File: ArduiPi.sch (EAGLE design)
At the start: 59 parts, among them IC1 DS2482-100S, IC2 AVR-MEGA8-PPTH, J1 VIN, J3 ISP, Q1 BS170, Q2 BS170, Q3 BS170, Q4 BS170, U1 LD1117 3V3, U2 78M05, U3 TXB0108, U4 TXB0108, Y1 16MHz

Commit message: Final Design
Final Design
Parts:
- removed $0000002: 22pF, SparkFun:CAPPTH2
- removed $5: 0.1uF, SparkFun:CAPPTH2
- removed JP3: PI I/O, adafruit:PINHD-1X8BIG
- removed JP4: 1-Wire, adafruit:PINHD-1X3
- removed P1, P2: (no value), Seeedstudio-Discreter.rpt:PAD-SOLDERJUMPER-2WAYT
- removed R13, R20: 10k, SparkFun:RESISTORAXIAL-0.3
- removed RASPBERRY: RASPBERRYPI_BB, microbuilder:RASPBERRYPI_BB
- removed S1: RESET, SparkFun:TAC_SWITCHPTH
- removed SERIAL-ARDUINO, SERIAL-PI: GROVE, Connector:TWIG-2.0-LEADED
- removed Y1: 16MHz, SparkFun:CRYSTALHC49US
- added ARDUINO-SERIAL, PI-SERIAL: GROVE, Connector:TWIG-2.0-LEADED
- added C13, C14, C15, C16: 0.1uF, resistor:C-EUC0603
- added D1: 1N4004, adafruit:1N4004
- added I2C-OLED, PC1, POWER: DNP, Seeedstudio-Connector:HEADER-6P-2.54
- added J10: ICSP, SparkFun:AVR_SPI_PRG_6PTH
- added J11: DNP, Seeedstudio-Connector:HEADER-4P-80/40MIL
- added J12, J13, PB1, PD1, SPI-OLED, SPI-OLED-PI: DNP, Seeedstudio-Connector:HEADER-8P-2.54
- added J2, J4, J5, J6, J7, J8: DNP, Seeedstudio-Connector:HEADER-3P-2.54
- added J9: DC-044-AH, For_Test_Albert:DC-044
- added K1: RESET, Seeedstudio-Discrete.rpt:BOTTON-2P-90
- added LED1: BLUE, led:LEDCHIP-LED0603
- added LED2: RED, led:LEDCHIP-LED0603
- added PAD1: PAD1, Seeedstudio-Discreter.rpt:PAD-SOLDERJUMPER-2WAYS
- added PAD2: PAD0, Seeedstudio-Discreter.rpt:PAD-SOLDERJUMPER-2WAYS
- added PI-P1: PI-P1, pi:RASPBERRYPI_BV2
- added PLED1: PLED1, Seeedstudio-Discreter.rpt:PAD-SOLDERJUMPER-2WAYS
- added PLED2: PLED2, Seeedstudio-Discreter.rpt:PAD-SOLDERJUMPER-2WAYS
- added PSSPI: PSSPI, Seeedstudio-Discreter.rpt:PAD-SOLDERJUMPER-2WAYS
- added PVDD: PVDD, Seeedstudio-Discreter.rpt:PAD-SOLDERJUMPERNC
- added Q5: BSS84, transistor-small-signal:BSS84
- added R10: 180, resistor:R-EU_R0805
- added R4: 4.7K, resistor:R-EU_R0805
- added R7, R8: 10k, resistor:R-EU_R0603
- added R9: 120, resistor:R-EU_R0805
- added U5: TXB0108, adafruit:TXB0108PWR
- C1: value 47uF -> 0.1uF; device SparkFun:CAP_POLPTH1 -> Seeedstudio-Discrete.rpt:C'1.4'
- C10: value 22pF -> 0.1uF; device SparkFun:CAPPTH2 -> Seeedstudio-Discrete.rpt:C'1.4'
- C11, C12: device SparkFun:CAPPTH2 -> resistor:C-EUC0603
- C2, C3: value 0.1uF -> 22pF; device SparkFun:CAPPTH2 -> Seeedstudio-Discrete.rpt:C'1.4'
- C4, C5, C8: device SparkFun:CAPPTH2 -> Seeedstudio-Discrete.rpt:C'1.4'
- C6: value 0.1uF -> 47uF; device SparkFun:CAPPTH2 -> SparkFun:CAP_POLPTH2
- C7: value 0.1uF -> 10uF; device SparkFun:CAPPTH2 -> SparkFun:CAP_POLPTH2
- C9: value 10uF -> 0.1uF; device SparkFun:CAP_POLPTH1 -> resistor:C-EUC0603
- IC1: value DS2482-100S -> AVR-MEGA8-PPTH; device 1wire:DS2482-100S -> SparkFun:AVR-MEGA8-PPTH
- IC2: value AVR-MEGA8-PPTH -> DS2482-100S; device SparkFun:AVR-MEGA8-PPTH -> 1wire:DS2482-100S
- J1: value VIN -> Teleinfo; device SparkFun:POWER_JACKPTH_LOCK -> Seeedstudio-Connector:HEADER-2P-2.54
- J3: value ISP -> DNP; device SparkFun:AVR_SPI_PRG_6PTH -> Seeedstudio-Connector:HEADER-3P-2.54
- JP2: value PI I/O -> 1-Wire; device adafruit:PINHD-1X8BIG -> adafruit:PINHD-1X3
- PCLK: value (none) -> PCLK
- PMISO: value (none) -> PMISO
- PMOSI: value (none) -> PMOSI
- PRX: value (none) -> PRX
- PSCL: value (none) -> PSCL
- PSDA: value (none) -> PSDA
- PSS: value (none) -> PSS; device Seeedstudio-Discreter.rpt:PAD-SOLDERJUMPERNC -> Seeedstudio-Discreter.rpt:PAD-SOLDERJUMPER-2WAYS
- PTX: value (none) -> PTX
- Q1, Q2, Q3, Q4: value BS170 -> BSS138; device transistor-small-signal:BS170 -> Seeedstudio-Discreter.rpt:MOSFET-N-SOT23
- R1: value 10k -> 1.2k; device SparkFun:RESISTORAXIAL-0.3 -> resistor:R-EU_R0805
- R2: value 1.2k -> 10k; device SparkFun:RESISTORAXIAL-0.3 -> resistor:R-EU_R0805
- R3: device SparkFun:RESISTORAXIAL-0.3 -> resistor:R-EU_R0805
- R5: value 10k -> 4.7K; device SparkFun:RESISTORAXIAL-0.3 -> resistor:R-EU_R0805
- R6: device SparkFun:RESISTORAXIAL-0.3 -> resistor:R-EU_R0603
- STINFO: value (none) -> STINFO; device Seeedstudio-Discreter.rpt:PAD-SOLDERJUMPER-2WAYT -> Seeedstudio-Discreter.rpt:PAD-SOLDERJUMPER-2WAYS
- U1: value LD1117 3V3 -> 78M05; device Seeedstudio-IC:LD1117SOT223 -> SeedStudio-IC:78M05-TO252
- U2: value 78M05 -> LD1117 3V3; device SeedStudio-IC:78M05-TO252 -> Seeedstudio-IC:LD1117SOT223
- U3: value TXB0108 -> TXB0104; device adafruit:TXB0108PWR -> adafruit:TXB0104PWR
- X1: value (none) -> 16Mhz; device _c2h:CON-CLAMP-2 -> Seeedstudio-Discrete.rpt:CRYSTAL-HC49S
- renumbered SCL to PSCL, SDA to PSDA
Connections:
- new net GPIO28: PI-P1.GPIO8, U3.A1
- new net GPIO29: PI-P1.GPIO9, U3.A2
- new net GPIO30: PI-P1.GPIO10, U3.A3
- new net GPIO31: PI-P1.GPIO11, U3.A4
- new net IO28: J11.P$1, U3.B1
- new net IO29: J11.P$2, U3.B2
- new net IO30: J11.P$3, U3.B3
- new net IO31: J11.P$4, U3.B4
- new net N$14: J1.2, R1.2
- new net N$15: IC2G$1.PCT, Q5.G
- new net N$16: PLED1.2, R9.1
- new net N$17: LED1.A, R9.2
- new net N$18: LED2.A, R10.2
- new net N$19: R6.1, U3.OE
- new net N$20: PLED2.2, R10.1
- new net SSPI: PSSPI.2, SPI-OLED-PI.8
- net 3V3: now also POWER.5
- net 3V3-EXT: now also C10.2, U2.OUT, U2.TAB; no longer C7.1, U1.TAB
- net 3V3-PI: now also C11.1, C12.1, C13.1, PI-P1.3.3V@1, PI-P1.3.3V@2, Q3.G, R7.2, R8.2, U5.VCCA; no longer C2.1, C3.1, Q2.G, R5.2, RASPBERRY.3V3-PI
- net 5V-EXT: now also C7.+, C8.2, PLED2.1, PVDD.2, U1.OUT, U2.IN; no longer C12.1, C9.+, U1.IN, U2.OUT
- net 5V-PI: now also PI-P1.5.0V@1, PI-P1.5.0V@2, PLED2.3; no longer RASPBERRY.5V-PI
- net AD0: now also IC1.PC0(ADC0), PC1.1; no longer IC2.PC0(ADC0)
- net AD1: now also IC1.PC1(ADC1), PC1.2; no longer IC2.PC1(ADC1)
- net AD2: now also IC1.PC2(ADC2), PC1.3; no longer IC2.PC2(ADC2)
- net AD3: now also IC1.PC3(ADC3), PC1.4; no longer IC2.PC3(ADC3)
- net AD4/SDA: now also IC1.PC4(ADC4/SDA), PC1.5; no longer IC2.PC4(ADC4/SDA)
- net AD5/SCL: now also IC1.PC5(ADC5/SCL), PC1.6; no longer IC2.PC5(ADC5/SCL)
- net AREF: now also C5.2, PB1.8; no longer C11.1
- net CE0: now also J13.6, PSS.3, PSSPI.3, U5.B6; no longer JP3.6, PSS.1, U4.B6
- net CE1: now also J13.7, PSS.1, PSSPI.1, U5.B7; no longer JP3.7, U4.B7
- net CE3: now also J13.8, U5.B8; no longer JP3.8, U4.B8
- net D0/RX-I: now also ARDUINO-SERIAL.1, IC1.PD0(RXD), PD1.1; no longer IC2.PD0(RXD)
- net D1/TX-O: now also ARDUINO-SERIAL.2, IC1.PD1(TXD), PD1.2; no longer IC2.PD1(TXD)
- net D10/SS: now also IC1.PB2(SS/OC1B), J6.P$3, PB1.3, SPI-OLED.8; no longer IC2.PB2(SS/OC1B)
- net D11/MOSI: now also IC1.PB3(MOSI/OC2), J10.4, J7.P$3, PB1.4, SPI-OLED.4; no longer IC2.PB3(MOSI/OC2), J3.4
- net D12/MISO: now also IC1.PB4(MISO), J10.1, PB1.5; no longer IC2.PB4(MISO), J3.1
- net D13/SCK: now also IC1.PB5(SCK), J10.3, PB1.6, PLED1.1, SPI-OLED.5; no longer IC2.PB5(SCK), J3.3
- net D2: now also IC1.PD2(INT0), PD1.3, PLED1.3; no longer IC2.PD2(INT0)
- net D3: now also IC1.PD3(INT1), J2.P$3, PD1.4; no longer IC2.PD3(INT1)
- net D4: now also I2C-OLED.4, IC1.PD4(XCK/T0), PD1.5; no longer IC2.PD4(XCK/T0)
- net D5: now also IC1.PD5(T1), J3.P$3, PD1.6; no longer IC2.PD5(T1)
- net D6: now also IC1.PD6(AIN0), J4.P$3, PD1.7; no longer IC2.PD6(AIN0)
- net D7: now also IC1.PD7(AIN1), PD1.8, SPI-OLED.7; no longer IC2.PD7(AIN1)
- net D8: now also IC1.PB0(ICP), PB1.1, SPI-OLED.6; no longer IC2.PB0(ICP)
- net D9: now also IC1.PB1(OC1A), J5.P$3, PB1.2; no longer IC2.PB1(OC1A)
- net DTR: now also C1.2; no longer C8.1
- net GND: now also ARDUINO-SERIAL.4, C13.2, C14.2, C15.2, C16.2, C6.-, C7.-, C8.1, C9.2, I2C-OLED.3, IC1.AGND, IC1.GND@1, IC2P.GND, J10.6, J2.P$2, J3.P$2, J4.P$2, J5.P$2, J6.P$2, J7.P$2, J8.P$2, J9.-, J9.CDN, JP2.3, K1.1, LED1.C, LED2.C, PAD1.1, PAD2.1, PB1.7, PI-P1.GND, PI-P1.GND@2, PI-P1.GND@3, PI-SERIAL.4, POWER.2, POWER.3, SPI-OLED-PI.1, SPI-OLED.1, U5.GND; no longer $0000002.1, $5.1, C1.-, C6.1, C7.2, C9.-, IC1P.GND, IC2.AGND, IC2.GND@1, J1.GND, J1.GNDBREAK, J3.6, P1.1, P2.1, RASPBERRY.GND, S1.1, S1.2, SERIAL-ARDUINO.4, SERIAL-PI.4
- net GPIO17: now also PI-P1.GPIO0, U4.A2; no longer RASPBERRY.GPIO0, U3.A2
- net GPIO18: now also PI-P1.GPIO1, U4.A3; no longer RASPBERRY.GPIO1, U3.A3
- net GPIO21: now also PI-P1.GPIO2, U4.A4; no longer RASPBERRY.GPIO2, U3.A4
- net GPIO22: now also PI-P1.GPIO3, U4.A5; no longer RASPBERRY.GPIO3, U3.A5
- net GPIO23: now also PI-P1.GPIO4, U4.A6; no longer RASPBERRY.GPIO4, U3.A6
- net GPIO24: now also PI-P1.GPIO5, U4.A7; no longer RASPBERRY.GPIO5, U3.A7
- net GPIO25: now also PI-P1.GPIO6, U4.A8; no longer RASPBERRY.GPIO6, U3.A8
- net GPIO4: now also PI-P1.GPIO7, U4.A1; no longer RASPBERRY.GPIO7, U3.A1
- net IO17: now also J12.2, U4.B2; no longer JP2.2, U3.B2
- net IO18: now also J12.3, J8.P$3, U4.B3; no longer JP2.3, U3.B3
- net IO21: now also J12.4, U4.B4; no longer JP2.4, U3.B4
- net IO22: now also J12.5, U4.B5; no longer JP2.5, U3.B5
- net IO23: now also J12.6, U4.B6; no longer JP2.6, U3.B6
- net IO24: now also J12.7, SPI-OLED-PI.6, U4.B7; no longer JP2.7, U3.B7
- net IO25: now also J12.8, SPI-OLED-PI.7, U4.B8; no longer JP2.8, U3.B8
- net IO4: now also J12.1, U4.B1; no longer JP2.1, U3.B1
- net MISO: now also J13.4, U5.B4; no longer JP3.4, U4.B4
- net MISO-PI: now also PI-P1.SPI_MISO, U5.A4; no longer RASPBERRY.SPI_MISO
- net MOSI: now also J13.3, SPI-OLED-PI.4, U5.B3; no longer JP3.3, U4.B3
- net MOSI-PI: now also PI-P1.SPI_MOSI, U5.A3; no longer RASPBERRY.SPI_MOSI
- net N$10: now also JP1.4, PVDD.1; no longer R2.2, X1-1.KL
- net N$11: now also IC2G$1.AD1, PAD1.2; no longer IC1G$1.AD1, P1.2
- net N$12: now also D1.A, J9.+; no longer U1.OUT
- net N$13: now also R8.1, U5.OE; no longer R6.1, U4.OE
- net N$2: now also IC2G$1.AD0, PAD2.2; no longer IC1G$1.AD0, P2.2
- net N$3: now also C3.1, IC1.PB7(XTAL2/TOSC2), X1.1; no longer $0000002.2, IC2.PB6(XTAL1/TOSC1), Y1.2
- net N$4: now also C2.1, IC1.PB6(XTAL1/TOSC1), X1.2; no longer C10.2, IC2.PB7(XTAL2/TOSC2), Y1.1
- net N$5: now also Q1.D; no longer Q2.D
- net N$6: now also Q2.D; no longer Q1.D
- net N$7: now also R7.1, U4.OE; no longer R5.1, U3.OE
- net N$8: now also R1.1; no longer R2.1
- net N$9: now also J1.1; no longer X1-2.KL
- net OW: now also IC2G$1.1W, JP2.2, Q5.D; no longer IC1G$1.1W, JP4.2
- net RESET: now also C1.1, IC1.PC6(/RESET), J10.5, K1.2, POWER.6, R2.2; no longer C8.2, IC2.PC6(/RESET), J3.5, R13.1, S1.3, S1.4
- net RXD: now also J13.2, PI-SERIAL.1, U5.B2; no longer JP3.2, U4.B2
- net RXD-PI: now also PI-P1.RXD, U5.A2; no longer RASPBERRY.RXD
- net SCL: now also I2C-OLED.5, IC2G$1.SCL, Q2.S, R5.1; no longer IC1G$1.SCL, Q1.S, R20.2
- net SCL-PI: now also PI-P1.SCL0; no longer RASPBERRY.SCL0
- net SCLK: now also J13.5, SPI-OLED-PI.5, U5.B5; no longer JP3.5, U4.B5
- net SCLK-PI: now also PI-P1.SPI_SCLK, U5.A5; no longer RASPBERRY.SPI_SCLK
- net SDA: now also I2C-OLED.6, IC2G$1.SDA, Q1.S, R4.1; no longer IC1G$1.SDA, Q3.S, R1.1
- net SDA-PI: now also PI-P1.SDA0, Q3.S; no longer Q2.S, RASPBERRY.SDA0
- net SPI_CE0: now also PI-P1.#SPI_CE0, U5.A6; no longer RASPBERRY.#SPI_CE0
- net SPI_CE1: now also PI-P1.#SPI_CE1, U5.A7; no longer RASPBERRY.#SPI_CE1
- net TXD: now also J13.1, PI-SERIAL.2, U5.B1; no longer JP3.1, U4.B1
- net TXD-PI: now also PI-P1.TXD, U5.A1; no longer RASPBERRY.TXD
- net VDD: now also ARDUINO-SERIAL.3, C14.1, C15.1, C16.1, C9.1, I2C-OLED.1, IC1.AVCC, IC1.VCC@1, IC2P.VDD, J10.2, J2.P$1, J3.P$1, J4.P$1, J5.P$1, J6.P$1, J7.P$1, J8.P$1, JP2.1, PAD1.3, PAD2.3, PI-SERIAL.3, POWER.4, Q2.G, Q5.S, R2.1, R4.2, R5.2, SPI-OLED-PI.3, SPI-OLED.3, U5.VCCB; no longer $5.2, C5.2, C6.2, IC1P.VDD, IC2.AVCC, IC2.VCC@1, J3.2, JP4.1, P1.3, P2.3, Q3.G, R1.2, R13.2, R20.1, SERIAL-ARDUINO.3, SERIAL-PI.3
- net VIN: now also C6.+, D1.C, POWER.1, U1.IN; no longer C1.+, J1.PWR, U2.IN
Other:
- note added: "Connectors (Grove, I2C, Serial, Oled, ...)"
- note added: "Grove"
- note added: "OLED"
- note added: "PWM"
- note added: "Raspberry P1"
- note added: "Raspberry P5 (REV. 2 Only)"
- note added: "Test Version 1.0"
- note removed: "I2C Grove + Dual Serial Grove (Pi and Arduino)"
- note removed: "Preliminary version 0.1"
- moved on the sheet: C11, C12, I2C, JP1, PCLK, PMISO, PMOSI, PRX, PTX, U4

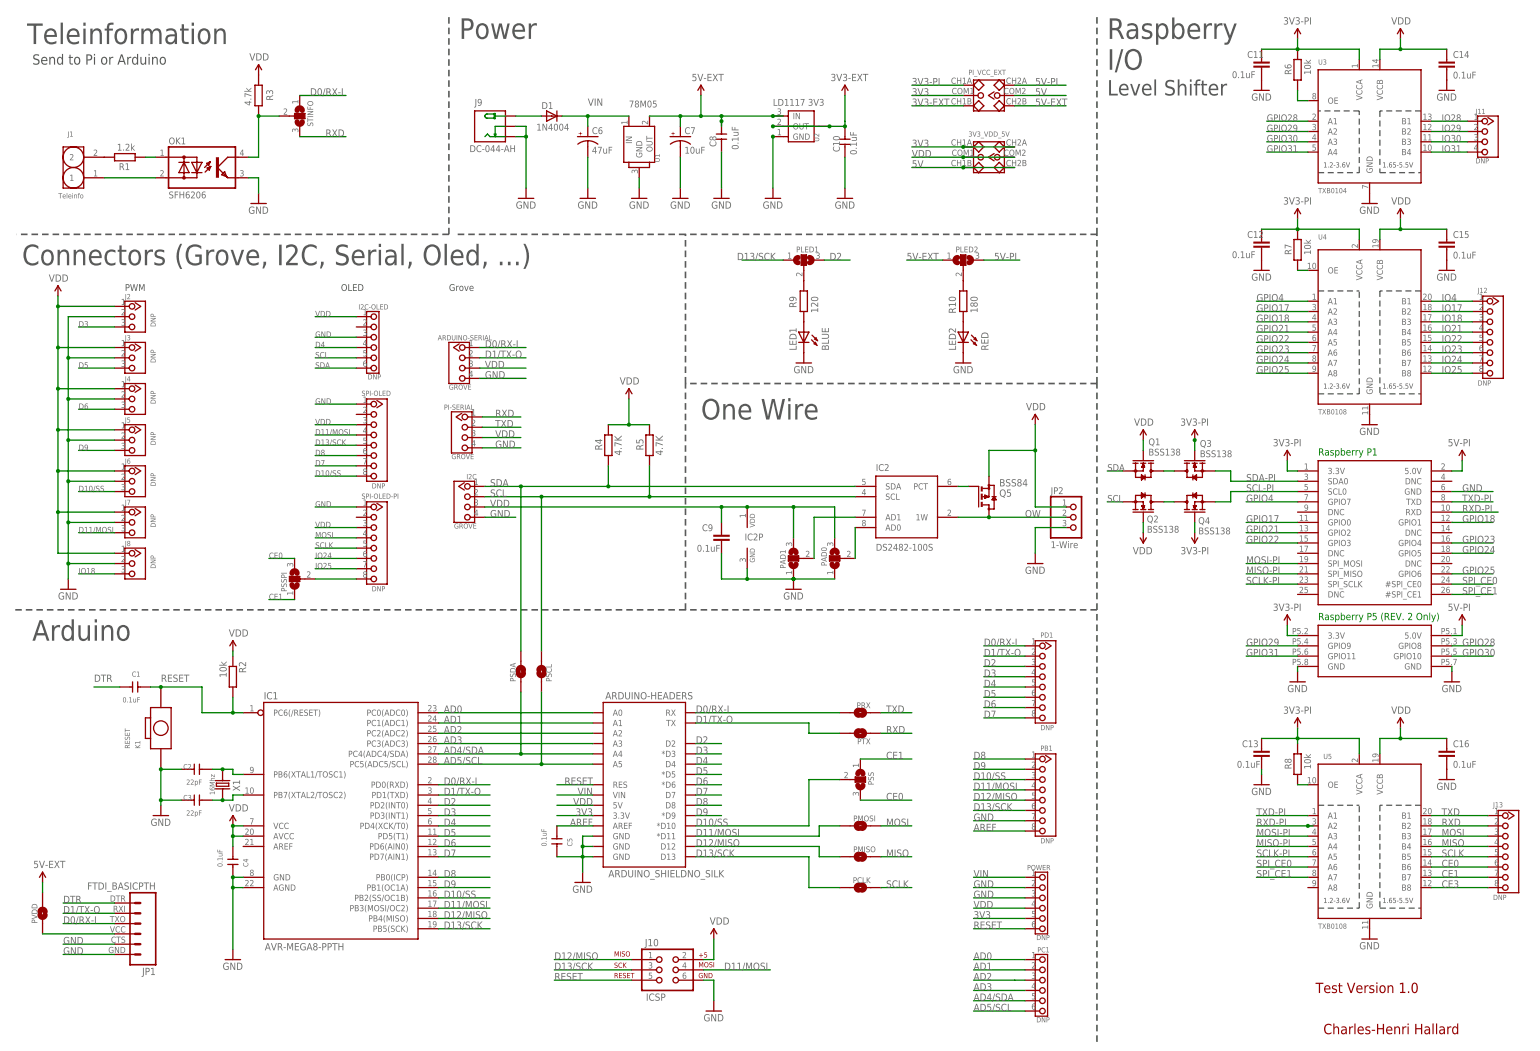
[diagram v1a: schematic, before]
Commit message: Added Pads
Added pads for One Wire and Prototyping area
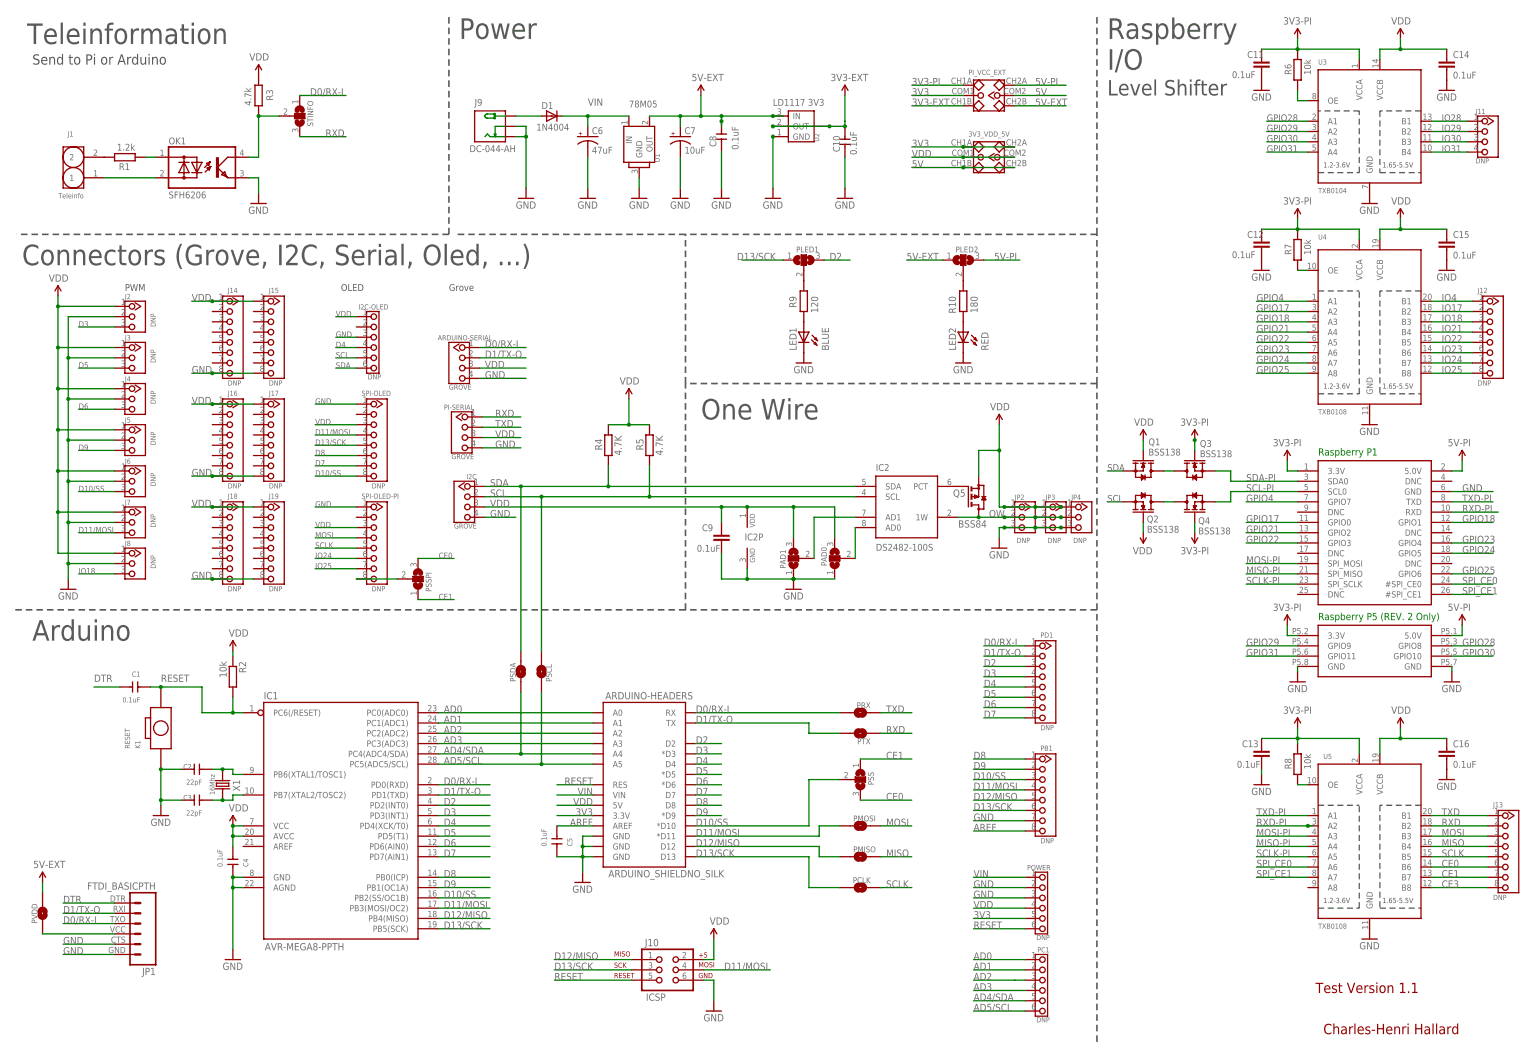
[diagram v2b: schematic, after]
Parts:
- added J14, J15, J16, J17, J18, J19: DNP, Seeedstudio-Connector:HEADER-8P-2.54
- added JP3, JP4: DNP, Seeedstudio-Connector:HEADER-3P-2.54
- JP2: value 1-Wire -> DNP; device adafruit:PINHD-1X3 -> Seeedstudio-Connector:HEADER-3P-2.54
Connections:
- net GND: now also J14.8, J15.8, J16.8, J17.8, J18.8, J19.8, JP2.P$3, JP3.P$3, JP4.P$3; no longer JP2.3
- net OW: now also JP2.P$2, JP3.P$2, JP4.P$2; no longer JP2.2
- net VDD: now also J14.1, J15.1, J16.1, J17.1, J18.1, J19.1, JP2.P$1, JP3.P$1, JP4.P$1; no longer JP2.1
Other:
- note added: "Test Version 1.1"
- note removed: "Test Version 1.0"
- moved on the sheet: Q5

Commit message: Prototype Board
ArduiPi First Prototype Board
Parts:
- removed ARDUINO-HEADERS: ARDUINO_SHIELDNO_SILK, SparkFun-Boards:ARDUINO_SHIELDNO_SILK
- removed J10: ICSP, SparkFun:AVR_SPI_PRG_6PTH
- removed J15, J16, J17, J18, J19: DNP, Seeedstudio-Connector:HEADER-8P-2.54
- removed JP1: FTDI_BASICPTH, SparkFun-Connectors:FTDI_BASICPTH
- removed K1: RESET, Seeedstudio-Discrete.rpt:BOTTON-2P-90
- added 24L01, 24L01-PI: DNP, Seeedstudio-Connector:HEADER-2X4P-2.54
- added PINT: PINT, Discrete:PAD-JUMPER-2P
- added PINTPI: PINTPI, Discrete:PAD-JUMPER-2P
- added PPWM, PSS1: (no value), Discrete:PAD-JUMPER-3P-40*40
- added RESET: TS-118E, Discrete:BUTTON-4P-REINFORCE'TS-118E'
- added U6: (no value), For_Test_Albert_v6:ARDUINO'W/-SILK
- C1, C10, C2, C3, C4, C5, C8: device Seeedstudio-Discrete.rpt:C'1.4' -> Discrete:C-0603
- C11, C12, C13, C14, C15, C16, C9: device resistor:C-EUC0603 -> Discrete:C-0603
- C6: value 47uF -> 16V_47uF; device SparkFun:CAP_POLPTH2 -> Discrete:CAP-AVX-C
- C7: value 10uF -> 10V_10uF; device SparkFun:CAP_POLPTH2 -> Discrete:CAP-AVX-A
- D1: value 1N4004 -> M7; device adafruit:1N4004 -> Discrete:D'SMA'
- I2C-OLED, PC1, POWER: device Seeedstudio-Connector:HEADER-6P-2.54 -> Connector:HEADER-6P-65/35MIL
- J11: device Seeedstudio-Connector:HEADER-4P-80/40MIL -> Connector:HEADER-4P-65/35MIL
- J12, J13, PB1, PD1, SPI-OLED, SPI-OLED-PI: device Seeedstudio-Connector:HEADER-8P-2.54 -> Connector:HEADER-8P-65/35MIL
- J14: value DNP -> (none); device Seeedstudio-Connector:HEADER-8P-2.54 -> Connector:HEADER-6P-65/35MIL
- J9: device For_Test_Albert:DC-044 -> Connector:JACK-DC-044
- LED1, LED2: device led:LEDCHIP-LED0603 -> Discrete:LED'0603'
- PAD1: value PAD1 -> (none); device Seeedstudio-Discreter.rpt:PAD-SOLDERJUMPER-2WAYS -> Discrete:PAD-JUMPER-3P-40*40; PARTNO (none) -> DNP
- PAD2: value PAD0 -> (none); device Seeedstudio-Discreter.rpt:PAD-SOLDERJUMPER-2WAYS -> Discrete:PAD-JUMPER-3P-40*40; PARTNO (none) -> DNP
- PCLK, PMISO, PMOSI, PRX, PSCL, PSDA, PTX, PVDD: device Seeedstudio-Discreter.rpt:PAD-SOLDERJUMPERNC -> Discrete:PAD-JUMPER-2P
- PLED1: value PLED1 -> (none); device Seeedstudio-Discreter.rpt:PAD-SOLDERJUMPER-2WAYS -> Discrete:PAD-JUMPER-3P-40*40; PARTNO (none) -> DNP
- PLED2: value PLED2 -> (none); device Seeedstudio-Discreter.rpt:PAD-SOLDERJUMPER-2WAYS -> Discrete:PAD-JUMPER-3P-40*40
- PSS: value PSS -> (none); device Seeedstudio-Discreter.rpt:PAD-SOLDERJUMPER-2WAYS -> Discrete:PAD-JUMPER-3P-40*40
- PSSPI: value PSSPI -> (none); device Seeedstudio-Discreter.rpt:PAD-SOLDERJUMPER-2WAYS -> Discrete:PAD-JUMPER-3P-40*40; PARTNO (none) -> DNP
- R1, R2, R3, R4, R5: device resistor:R-EU_R0805 -> Discrete:R-0603
- R10: value 180 -> 600; device resistor:R-EU_R0805 -> Discrete:R-0603
- R6, R7, R8: device resistor:R-EU_R0603 -> Discrete:R-0603
- R9: value 120 -> 360; device resistor:R-EU_R0805 -> Discrete:R-0603
- STINFO: value STINFO -> (none); device Seeedstudio-Discreter.rpt:PAD-SOLDERJUMPER-2WAYS -> Discrete:PAD-JUMPER-3P-40*40
- X1: device Seeedstudio-Discrete.rpt:CRYSTAL-HC49S -> Discrete:CRYSTAL'5032'
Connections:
- new net CSN: 24L01-PI.7, PSS1.C
- new net IRQ: 24L01-PI.5, 24L01.5, PINT.2, PINTPI.2
- new net N$21: J2.P$1, J3.P$1, J4.P$1, J5.P$1, J6.P$1, J7.P$1, J8.P$1, PPWM.C
- net 3V3: now also 24L01-PI.8, 24L01.8, U6.3V3; no longer ARDUINO-HEADERS.3.3V
- net 5V-EXT: now also PLED2.L; no longer PLED2.1
- net 5V-PI: now also PLED2.R; no longer PLED2.3
- net AD0: now also U6.PC0/AD0/D14; no longer ARDUINO-HEADERS.A0
- net AD1: now also U6.PC1/AD1/D15; no longer ARDUINO-HEADERS.A1
- net AD2: now also U6.PC2/AD2/D16; no longer ARDUINO-HEADERS.A2
- net AD3: now also U6.PC3/AD3/D17; no longer ARDUINO-HEADERS.A3
- net AD4/SDA: now also U6.PC4/AD4/D18/SDA; no longer ARDUINO-HEADERS.A4
- net AD5/SCL: now also U6.PC5/AD5/D19/SCL; no longer ARDUINO-HEADERS.A5
- net AREF: now also C5.1, U6.AREF; no longer ARDUINO-HEADERS.AREF, C5.2
- net CE0: now also PSS.R, PSS1.L, PSSPI.R; no longer PSS.3, PSSPI.3
- net CE1: now also PSS.L, PSS1.R, PSSPI.L; no longer PSS.1, PSSPI.1
- net D0/RX-I: now also J14.3, STINFO.L, U6.PD0/D0/RX; no longer ARDUINO-HEADERS.RX, JP1.3, STINFO.1
- net D1/TX-O: now also J14.2, U6.PD1/D1/TX; no longer ARDUINO-HEADERS.TX, JP1.2
- net D10/SS: now also PSS.C, U6.PB2/D10/SS/PWM; no longer ARDUINO-HEADERS.*D10, PSS.2, SPI-OLED.8
- net D11/MOSI: now also 24L01.6, U6.MOSI, U6.PB3/D11/MOSI/PWM; no longer ARDUINO-HEADERS.*D11, J10.4
- net D12/MISO: now also 24L01.4, U6.MISO, U6.PB4/D12/MISO; no longer ARDUINO-HEADERS.D12, J10.1
- net D13/SCK: now also 24L01.3, PLED1.L, U6.PB5/D13/SCK, U6.SCK; no longer ARDUINO-HEADERS.D13, J10.3, PLED1.1
- net D2: now also PINT.1, PLED1.R, U6.PD2/D2/INT0; no longer ARDUINO-HEADERS.D2, PLED1.3
- net D3: now also 24L01.2, U6.PD3/D3/INT1/PWM; no longer ARDUINO-HEADERS.*D3
- net D4: now also 24L01.7, U6.PD4/D4; no longer ARDUINO-HEADERS.D4
- net D5: now also U6.PD5/D5/PWM; no longer ARDUINO-HEADERS.*D5
- net D6: now also U6.PD6/D6/PWM; no longer ARDUINO-HEADERS.*D6
- net D7: now also U6.PD7/D7; no longer ARDUINO-HEADERS.D7
- net D8: now also U6.PB0/D8; no longer ARDUINO-HEADERS.D8
- net D9: now also SPI-OLED.8, U6.PB1/D9/PWM; no longer ARDUINO-HEADERS.*D9
- net DTR: now also J14.1; no longer JP1.1
- net GND: now also 24L01-PI.1, 24L01.1, C5.2, J14.5, J14.6, LED1.-, LED2.-, PAD1.L, PAD2.L, RESET.1, RESET.S1, RESET.S2, U6.GND, U6.GND@0, U6.GND@1, U6.GND@2; no longer ARDUINO-HEADERS.GND@0, ARDUINO-HEADERS.GND@1, ARDUINO-HEADERS.GND@2, C5.1, J10.6, J14.8, J15.8, J16.8, J17.8, J18.8, J19.8, JP1.5, JP1.6, K1.1, LED1.C, LED2.C, PAD1.1, PAD2.1
- net IO22: now also 24L01-PI.2
- net IO23: now also PINTPI.1
- net MISO: now also 24L01-PI.4
- net MOSI: now also 24L01-PI.6
- net N$1: now also STINFO.C; no longer STINFO.2
- net N$10: now also J14.4; no longer JP1.4
- net N$11: now also PAD1.C; no longer PAD1.2
- net N$12: now also D1.+; no longer D1.A
- net N$16: now also PLED1.C; no longer PLED1.2
- net N$17: now also LED1.+; no longer LED1.A
- net N$18: now also LED2.+; no longer LED2.A
- net N$2: now also PAD2.C; no longer PAD2.2
- net N$20: now also PLED2.C; no longer PLED2.2
- net RESET: now also RESET.2, U6.RESET, U6.RST; no longer ARDUINO-HEADERS.RES, J10.5, K1.2
- net RXD: now also STINFO.R; no longer STINFO.3
- net SCLK: now also 24L01-PI.3
- net SSPI: now also PSSPI.C; no longer PSSPI.2
- net VDD: now also PAD1.R, PAD2.R, PPWM.L, U6.5V, U6.VCC; no longer ARDUINO-HEADERS.5V, J10.2, J14.1, J15.1, J16.1, J17.1, J18.1, J19.1, J2.P$1, J3.P$1, J4.P$1, J5.P$1, J6.P$1, J7.P$1, J8.P$1, PAD1.3, PAD2.3
- net VIN: now also D1.-, PPWM.R, U6.VIN; no longer ARDUINO-HEADERS.VIN, D1.C
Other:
- note added: "Connectors"
- note added: "Test Version 1.3"
- note added: "nrf24L01"
- note removed: "Connectors (Grove, I2C, Serial, Oled, ...)"
- note removed: "Test Version 1.1"
- moved on the sheet: ARDUINO-SERIAL, C1, C2, C3, C4, C5, I2C, IC1, IC2P, J2, J3, J4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
